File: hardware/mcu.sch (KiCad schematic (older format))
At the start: 26 parts

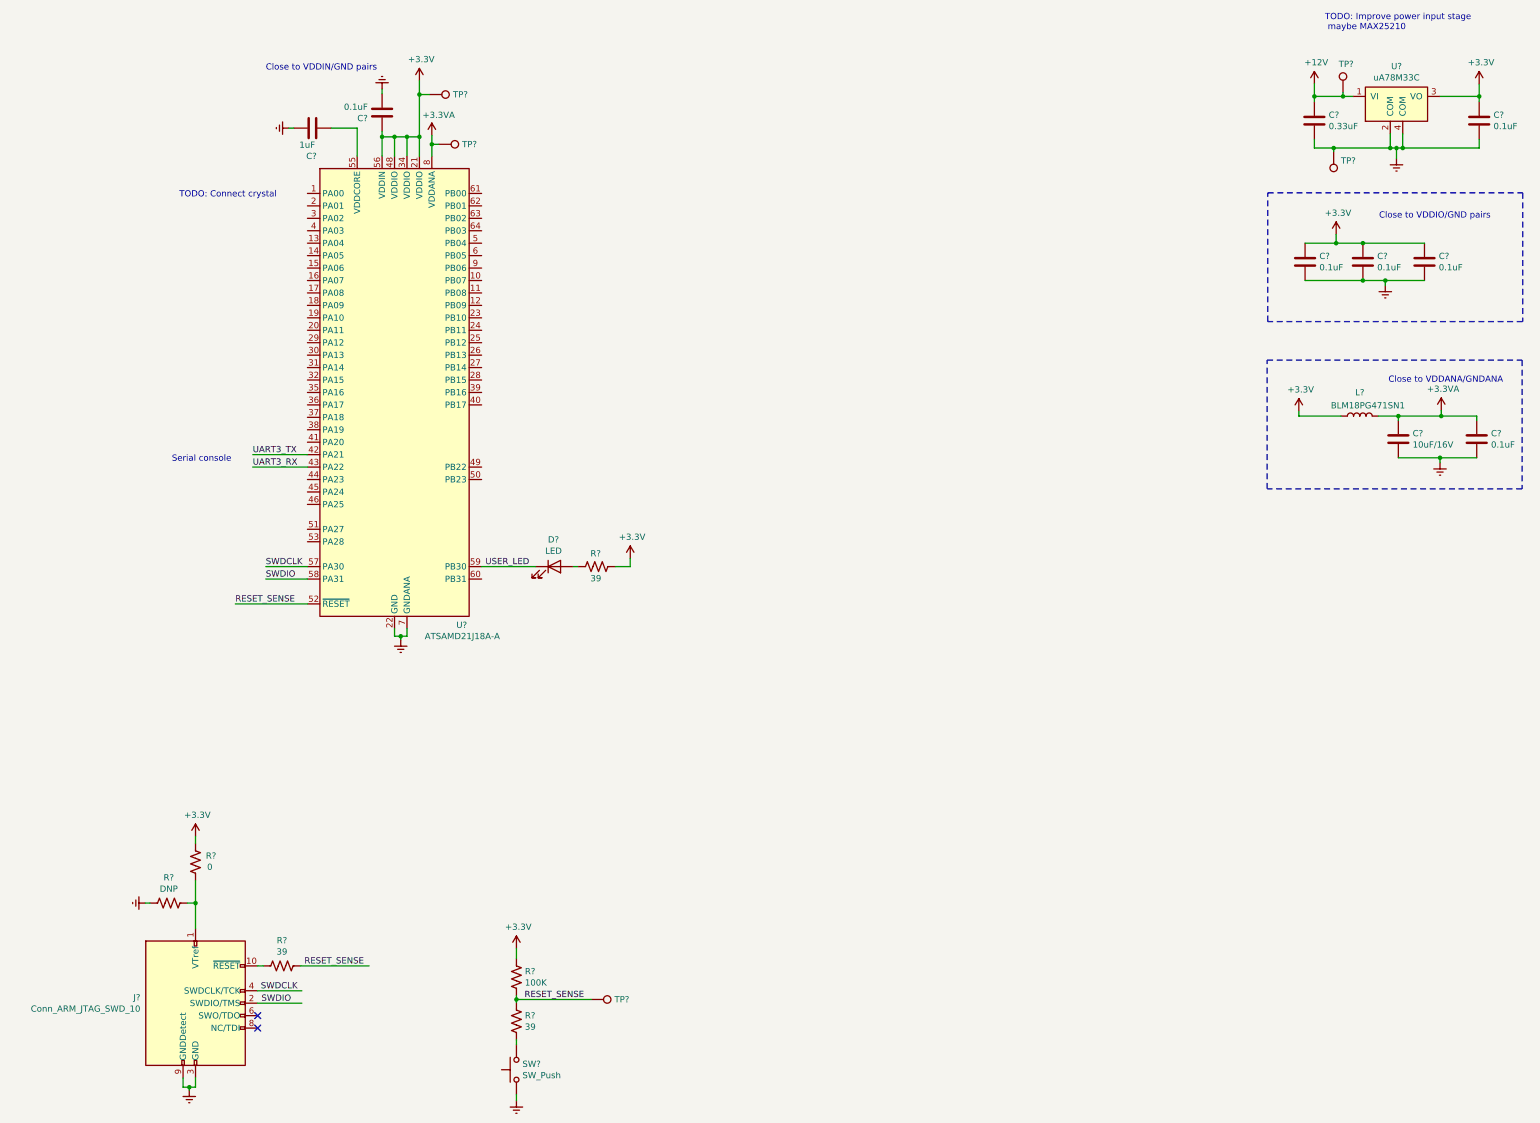
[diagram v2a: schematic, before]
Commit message: hardware: update MCU footprints
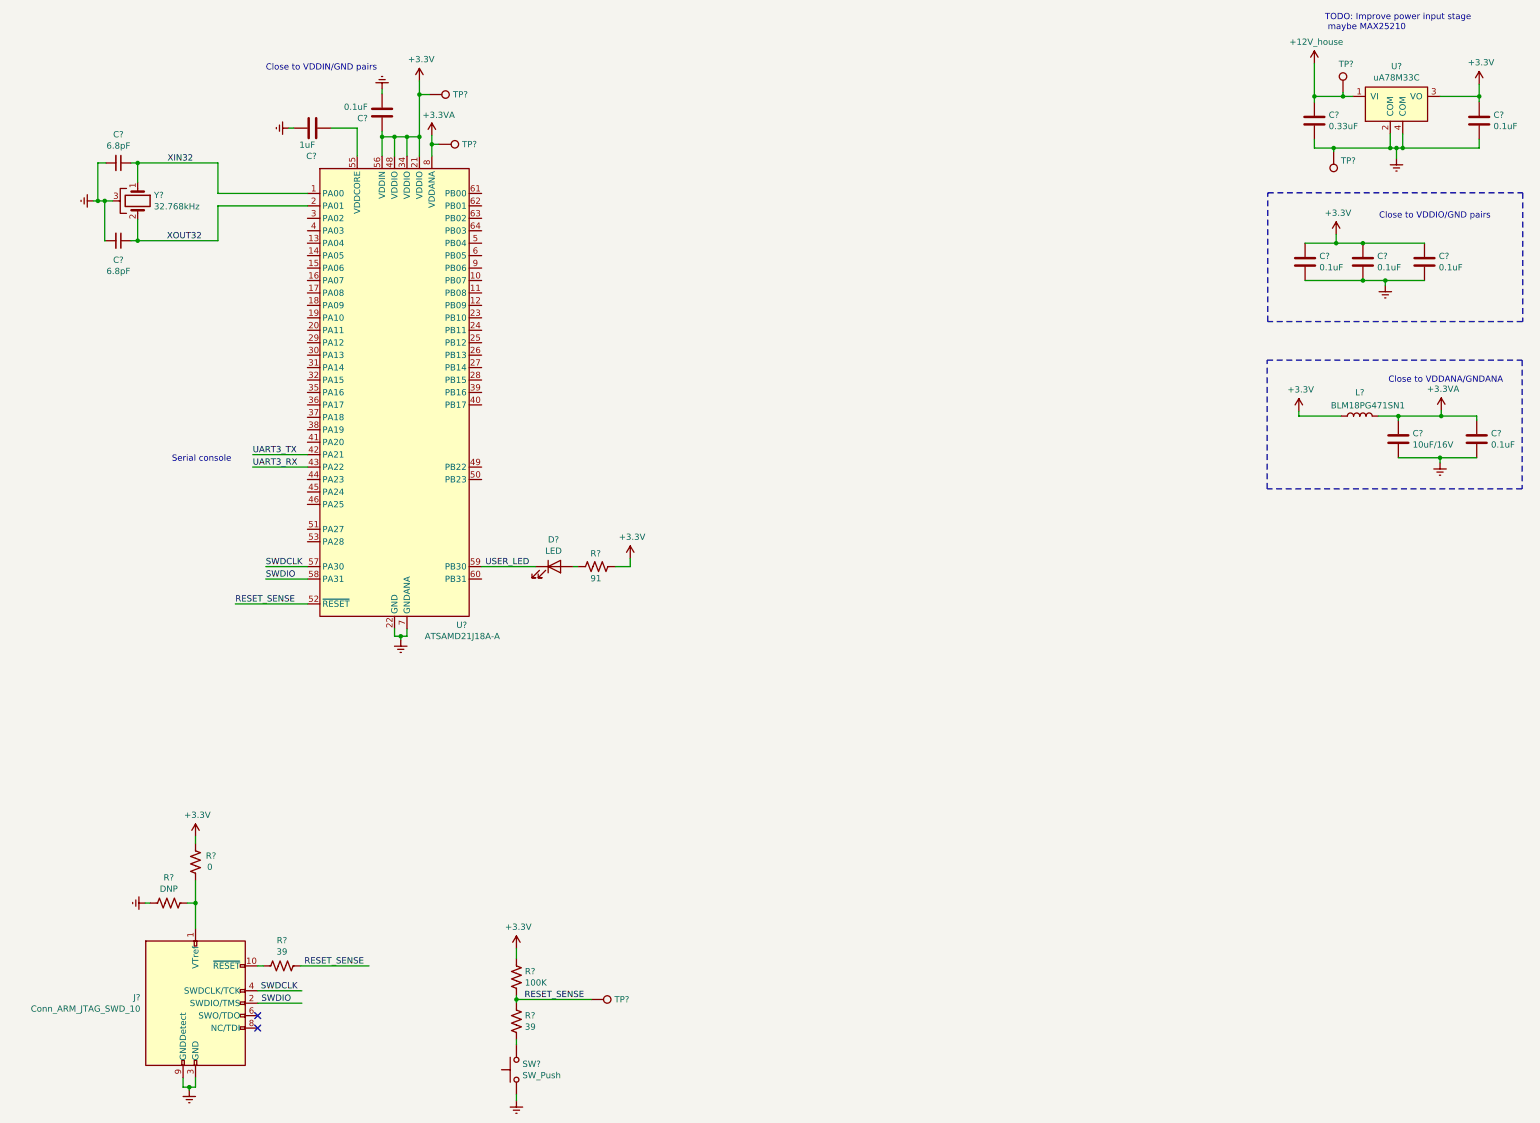
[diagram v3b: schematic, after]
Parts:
- added C? (x2): 6.8pF, Capacitor_SMD:C_0805_2012Metric_Pad1.18x1.45mm_HandSolder, symbol Device:C_Small
- added Y?: 32.768kHz, Crystal:Crystal_SMD_MicroCrystal_MS1V-T1K, symbol Device:Crystal_GND3
- C? (x9): footprint (none) -> Capacitor_SMD:C_0805_2012Metric_Pad1.18x1.45mm_HandSolder
- D?: footprint (none) -> LED_SMD:LED_0805_2012Metric_Pad1.15x1.40mm_HandSolder
- R? (x5): footprint (none) -> Resistor_SMD:R_0805_2012Metric_Pad1.20x1.40mm_HandSolder
- R?: value 39 -> 91; footprint (none) -> Resistor_SMD:R_0805_2012Metric_Pad1.20x1.40mm_HandSolder
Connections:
- net labels added: +12V_house, XIN32, XOUT32
- net labels removed: +12V
- wire segments 90 -> 107
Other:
- note removed: "TODO: Connect crystal"
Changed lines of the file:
@@
 $Descr A3 16535 11693
 encoding utf-8
-Sheet 5 6
+Sheet 5 5
 Title ""
 Date ""
@@
 $EndComp
 $Comp
-L power:+12V #PWR?
-U 1 1 60776846
-P 11710 1785
-F 0 "#PWR?" H 11710 1635 50  0001 C CNN
-F 1 "+12V" H 11725 1958 50  0000 C CNN
-F 2 "" H 11710 1785 50  0001 C CNN
-F 3 "" H 11710 1785 50  0001 C CNN
-	1    11710 1785
-	1    0    0    -1
-$EndComp
-$Comp
 L Device:C C?
 U 1 1 60780267
@@
 F 0 "C?" H 13150 2126 50  0000 L CNN
 F 1 "0.1uF" H 13150 2035 50  0000 L CNN
-F 2 "" H 13073 1930 50  0001 C CNN
+F 2 "Capacitor_SMD:C_0805_2012Metric_Pad1.18x1.45mm_HandSolder" H 13073 1930 50  0001 C CNN
 F 3 "~" H 13035 2080 50  0001 C CNN
 	1    13035 2080
@@
 F 0 "C?" H 11825 2126 50  0000 L CNN
 F 1 "0.33uF" H 11825 2035 50  0000 L CNN
-F 2 "" H 11748 1930 50  0001 C CNN
+F 2 "Capacitor_SMD:C_0805_2012Metric_Pad1.18x1.45mm_HandSolder" H 11748 1930 50  0001 C CNN
 F 3 "~" H 11710 2080 50  0001 C CNN
 	1    11710 2080
@@
 	12020 1885 11940 1885
 Connection ~ 11710 1885
-Wire Wire Line
-	11710 1885 11710 1785
 Wire Wire Line
 	11710 2230 11710 2300
@@
 F 0 "C?" H 11750 3261 50  0000 L CNN
 F 1 "0.1uF" H 11750 3170 50  0000 L CNN
-F 2 "" H 11673 3065 50  0001 C CNN
+F 2 "Capacitor_SMD:C_0805_2012Metric_Pad1.18x1.45mm_HandSolder" H 11673 3065 50  0001 C CNN
 F 3 "~" H 11635 3215 50  0001 C CNN
 	1    11635 3215
@@
 F 0 "C?" H 12215 3261 50  0000 L CNN
 F 1 "0.1uF" H 12215 3170 50  0000 L CNN
-F 2 "" H 12138 3065 50  0001 C CNN
+F 2 "Capacitor_SMD:C_0805_2012Metric_Pad1.18x1.45mm_HandSolder" H 12138 3065 50  0001 C CNN
 F 3 "~" H 12100 3215 50  0001 C CNN
 	1    12100 3215
@@
 F 0 "C?" H 12710 3261 50  0000 L CNN
 F 1 "0.1uF" H 12710 3170 50  0000 L CNN
-F 2 "" H 12633 3065 50  0001 C CNN
+F 2 "Capacitor_SMD:C_0805_2012Metric_Pad1.18x1.45mm_HandSolder" H 12633 3065 50  0001 C CNN
 F 3 "~" H 12595 3215 50  0001 C CNN
 	1    12595 3215
@@
 F 0 "C?" H 4330 2061 50  0000 L CNN
 F 1 "0.1uF" H 4330 1970 50  0000 L CNN
-F 2 "" H 4253 1865 50  0001 C CNN
+F 2 "Capacitor_SMD:C_0805_2012Metric_Pad1.18x1.45mm_HandSolder" H 4253 1865 50  0001 C CNN
 F 3 "~" H 4215 2015 50  0001 C CNN
 	1    4215 2015
@@
 F 0 "C?" V 3880 2090 50  0000 L CNN
 F 1 "1uF" V 3790 2035 50  0000 L CNN
-F 2 "" H 3693 1990 50  0001 C CNN
+F 2 "Capacitor_SMD:C_0805_2012Metric_Pad1.18x1.45mm_HandSolder" H 3693 1990 50  0001 C CNN
 F 3 "~" H 3655 2140 50  0001 C CNN
 	1    3655 2140
@@
 F 0 "C?" H 12500 4686 50  0000 L CNN
 F 1 "10uF/16V" H 12500 4595 50  0000 L CNN
-F 2 "" H 12423 4490 50  0001 C CNN
+F 2 "Capacitor_SMD:C_0805_2012Metric_Pad1.18x1.45mm_HandSolder" H 12423 4490 50  0001 C CNN
 F 3 "~" H 12385 4640 50  0001 C CNN
 	1    12385 4640
@@
 F 0 "C?" H 13130 4686 50  0000 L CNN
 F 1 "0.1uF" H 13130 4595 50  0000 L CNN
-F 2 "" H 13053 4490 50  0001 C CNN
+F 2 "Capacitor_SMD:C_0805_2012Metric_Pad1.18x1.45mm_HandSolder" H 13053 4490 50  0001 C CNN
 F 3 "~" H 13015 4640 50  0001 C CNN
 	1    13015 4640
@@
 F 0 "R?" H 5363 9366 50  0000 L CNN
 F 1 "39" H 5363 9275 50  0000 L CNN
-F 2 "" V 5335 9310 50  0001 C CNN
+F 2 "Resistor_SMD:R_0805_2012Metric_Pad1.20x1.40mm_HandSolder" V 5335 9310 50  0001 C CNN
 F 3 "~" H 5295 9320 50  0001 C CNN
 	1    5295 9320
@@
 F 0 "R?" H 5363 9011 50  0000 L CNN
 F 1 "100K" H 5363 8920 50  0000 L CNN
-F 2 "" V 5335 8955 50  0001 C CNN
+F 2 "Resistor_SMD:R_0805_2012Metric_Pad1.20x1.40mm_HandSolder" V 5335 8955 50  0001 C CNN
 F 3 "~" H 5295 8965 50  0001 C CNN
 	1    5295 8965
@@
 F 0 "R?" V 3205 8875 50  0000 C CNN
 F 1 "39" V 3296 8875 50  0000 C CNN
-F 2 "" V 3450 8865 50  0001 C CNN
+F 2 "Resistor_SMD:R_0805_2012Metric_Pad1.20x1.40mm_HandSolder" V 3450 8865 50  0001 C CNN
 F 3 "~" H 3410 8875 50  0001 C CNN
 	1    3410 8875
@@
 Wire Wire Line
 	3615 5665 3280 5665
-Text Notes 2585 2705 0    50   ~ 0
-TODO: Connect crystal
 $Comp
 L Device:R_US R?
@@
 P 5940 5665
 F 0 "R?" V 5835 5615 50  0000 L CNN
-F 1 "39" V 6035 5615 50  0000 L CNN
-F 2 "" V 5980 5655 50  0001 C CNN
+F 1 "91" V 6035 5615 50  0000 L CNN
+F 2 "Resistor_SMD:R_0805_2012Metric_Pad1.20x1.40mm_HandSolder" V 5980 5655 50  0001 C CNN
 F 3 "~" H 5940 5665 50  0001 C CNN
 	1    5940 5665
@@
 F 0 "D?" H 5593 5882 50  0000 C CNN
 F 1 "LED" H 5593 5791 50  0000 C CNN
-F 2 "" H 5600 5665 50  0001 C CNN
+F 2 "LED_SMD:LED_0805_2012Metric_Pad1.15x1.40mm_HandSolder" H 5600 5665 50  0001 C CNN
 F 3 "~" H 5600 5665 50  0001 C CNN
 	1    5600 5665
@@
 F 0 "R?" V 2295 8370 50  0000 C CNN
 F 1 "DNP" V 2386 8370 50  0000 C CNN
-F 2 "" V 2540 8360 50  0001 C CNN
+F 2 "Resistor_SMD:R_0805_2012Metric_Pad1.20x1.40mm_HandSolder" V 2540 8360 50  0001 C CNN
 F 3 "~" H 2500 8370 50  0001 C CNN
 	1    2500 8370
@@
 F 0 "R?" H 2590 7990 50  0000 C CNN
 F 1 "0" H 2600 8080 50  0000 C CNN
-F 2 "" V 2755 8030 50  0001 C CNN
+F 2 "Resistor_SMD:R_0805_2012Metric_Pad1.20x1.40mm_HandSolder" V 2755 8030 50  0001 C CNN
 F 3 "~" H 2715 8040 50  0001 C CNN
 	1    2715 8040
@@
 Wire Wire Line
 	2715 7835 2715 7890
+$Comp
+L switchboard:+12V_house #PWR?
+U 1 1 6090ADE3
+P 11710 1620
+F 0 "#PWR?" H 11710 1470 50  0001 C CNN
+F 1 "+12V_house" H 11725 1793 50  0000 C CNN
+F 2 "" H 11710 1620 50  0001 C CNN
+F 3 "" H 11710 1620 50  0001 C CNN
+	1    11710 1620
+	1    0    0    -1
+$EndComp
+Wire Wire Line
+	11710 1620 11710 1885
+$Comp
+L Device:Crystal_GND3 Y?
+U 1 1 60810E0A
+P 2250 2725
+F 0 "Y?" V 2204 2856 50  0000 L CNN
+F 1 "32.768kHz" V 2295 2856 50  0000 L CNN
+F 2 "Crystal:Crystal_SMD_MicroCrystal_MS1V-T1K" H 2250 2725 50  0001 C CNN
+F 3 "~" H 2250 2725 50  0001 C CNN
+	1    2250 2725
+	0    1    1    0
+$EndComp
+$Comp
+L power:GNDREF #PWR?
+U 1 1 60813DFE
+P 1895 2725
+F 0 "#PWR?" H 1895 2475 50  0001 C CNN
+F 1 "GNDREF" V 1900 2597 50  0001 R CNN
+F 2 "" H 1895 2725 50  0001 C CNN
+F 3 "" H 1895 2725 50  0001 C CNN
+	1    1895 2725
+	0    1    1    0
+$EndComp
+$Comp
+L Device:C_Small C?
+U 1 1 6081B79D
+P 2095 2420
+F 0 "C?" V 1866 2420 50  0000 C CNN
+F 1 "6.8pF" V 1957 2420 50  0000 C CNN
+F 2 "Capacitor_SMD:C_0805_2012Metric_Pad1.18x1.45mm_HandSolder" H 2095 2420 50  0001 C CNN
+F 3 "~" H 2095 2420 50  0001 C CNN
+	1    2095 2420
+	0    1    1    0
+$EndComp
+$Comp
+L Device:C_Small C?
+U 1 1 6081BF7D
+P 2095 3045
+F 0 "C?" V 2250 3045 50  0000 C CNN
+F 1 "6.8pF" V 2340 3045 50  0000 C CNN
+F 2 "Capacitor_SMD:C_0805_2012Metric_Pad1.18x1.45mm_HandSolder" H 2095 3045 50  0001 C CNN
+F 3 "~" H 2095 3045 50  0001 C CNN
+	1    2095 3045
+	0    1    1    0
+$EndComp
+Wire Wire Line
+	2195 2420 2250 2420
+Wire Wire Line
+	2250 2420 2250 2575
+Wire Wire Line
+	2195 3045 2250 3045
+Wire Wire Line
+	2250 3045 2250 2875
+Wire Wire Line
+	1995 3045 1985 3045
+Wire Wire Line
+	1985 3045 1985 2725
+Connection ~ 1985 2725
+Wire Wire Line
+	1985 2725 2050 2725
+Wire Wire Line
+	1895 2725 1930 2725
+Wire Wire Line
+	1930 2725 1930 2420
+Connection ~ 1930 2725
+Wire Wire Line
+	1930 2725 1985 2725
+Wire Wire Line
+	1930 2420 1995 2420
+Wire Wire Line
+	3615 2665 2895 2665
+Wire Wire Line
+	2250 2420 2895 2420
+Wire Wire Line
+	2895 2420 2895 2665
+Connection ~ 2250 2420
+Wire Wire Line
+	2250 3045 2895 3045
+Wire Wire Line
+	2895 3045 2895 2765
+Wire Wire Line
+	2895 2765 3615 2765
+Connection ~ 2250 3045
+Text Label 2485 3045 0    50   ~ 0
+XOUT32
+Text Label 2490 2420 0    50   ~ 0
+XIN32
 $EndSCHEMATC
